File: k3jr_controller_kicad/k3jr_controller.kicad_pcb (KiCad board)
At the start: 2 copper layers, 161.3 x 40.6 mm, 80 parts, among them J1 CLK_IN, J17 MISO, J18 3V3, J19 SCK, J2 DAT_IN, J20 SPI, J21 MOSI, J22 RST, J23 GND, J24 I2C_ext1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

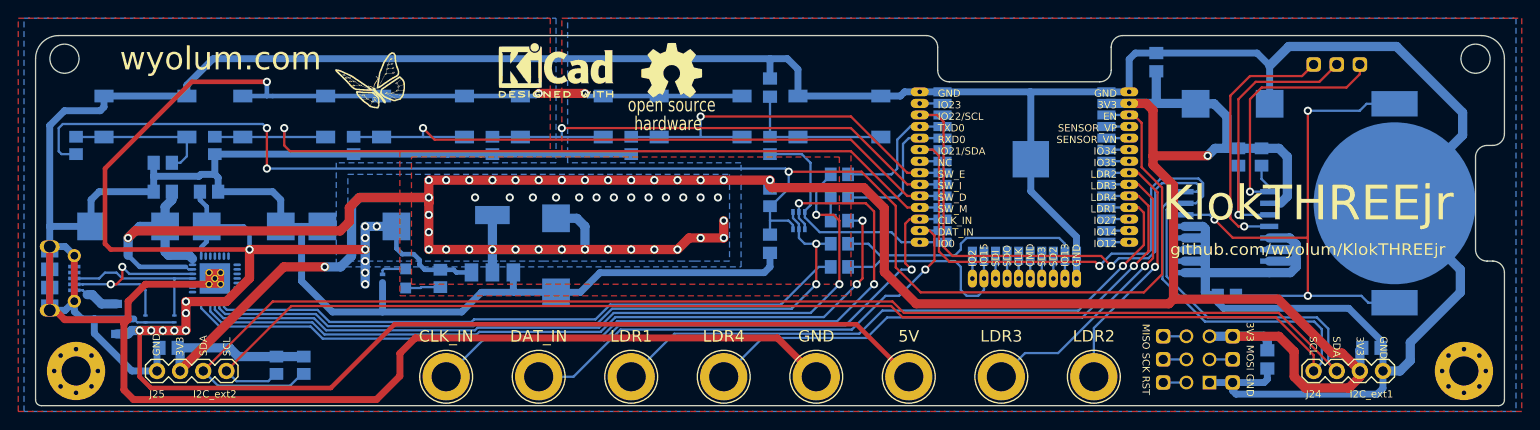
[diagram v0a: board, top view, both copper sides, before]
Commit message: correction to Kontroller and KlockTHREEjr
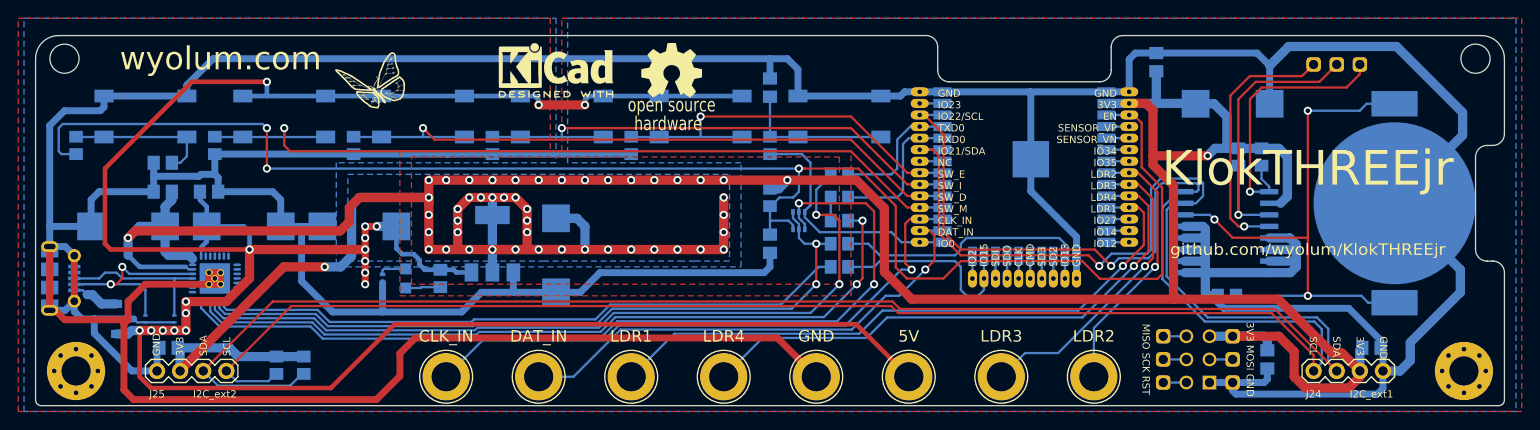
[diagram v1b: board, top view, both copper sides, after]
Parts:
- P1: footprint k3jr_controller_libs:USB_Micro-B_Molex-105017-0001_round -> k3jr_controller_libs:USB_Micro-B_Molex-105017-0001
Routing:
- net /3V3: track 393.0 -> 416.9 mm
- net /EN: track 173.7 -> 175.8 mm
- net /SCL: track 226.3 -> 224.6 mm
- net /5V: track 277.5 -> 278.7 mm
- net /SDA: track 234.7 -> 233.6 mm

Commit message: Kontroller layout/Gerber final
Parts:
- G1, G2, G3: moved to F.Cu
- G4, G5, G6: moved to B.Cu
- moved G4 59.4 mm to (136.8, 76.2), turned to 180 degrees
- moved G1 40.8 mm to (66.7, 52.1), turned to 0 degrees
- moved G5 27.7 mm to (120.0, 79.5), turned to 180 degrees
- moved G2 21.7 mm to (118.7, 55.9), turned to 0 degrees
- moved G3 15.8 mm to (132.1, 54.6), turned to 0 degrees
- moved G6 14.6 mm to (120.0, 69.2), turned to 180 degrees
- moved D3 1.52 mm to (66.0, 80.4)
- moved D4 1.52 mm to (62.9, 80.4)
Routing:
- net /5V: track 278.7 -> 288.3 mm
- net /3V3: track 416.9 -> 410.4 mm
- net GND: track 678.0 -> 684.0 mm
- net Net-(D1-Pad1): track 5.25 -> 10.4 mm, vias 0 -> 4
- net /esp_pwr_uart/USB_D-: track 21.7 -> 20.1 mm
- net /esp_pwr_uart/USB_D+: track 17.6 -> 16.1 mm
- net /EN: track 175.8 -> 174.4 mm
- net /SCL: track 224.6 -> 225.8 mm
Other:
- net class 10mil added: clearance 0.1016, trace_width 0.254, via_dia 0.9, via_drill 0.5
- net class 20mil added: clearance 0.1016, trace_width 0.508, via_dia 0.9, via_drill 0.5
- net class 30mil: clearance 0.2032 -> 0.1016
- net class 40mil: clearance 0.2032 -> 0.1016
- net class 8 mil: clearance 0.1016 -> 0.0381
- net class Default: clearance 0.2032 -> 0.1016
- rule trace_clearance: 0.2032 -> 0.1016
- rule trace_min: 0.1524 -> 0.08
- rule via_min_size: 0.762 -> 0.9
